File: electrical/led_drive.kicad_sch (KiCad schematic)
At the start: 0 parts

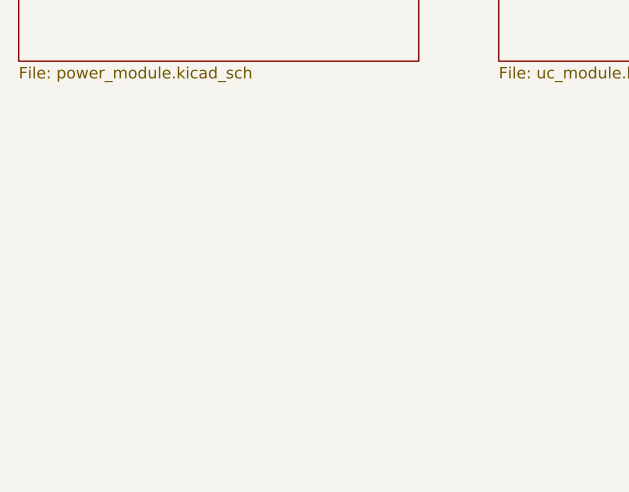
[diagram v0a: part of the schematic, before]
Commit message: Added more readme
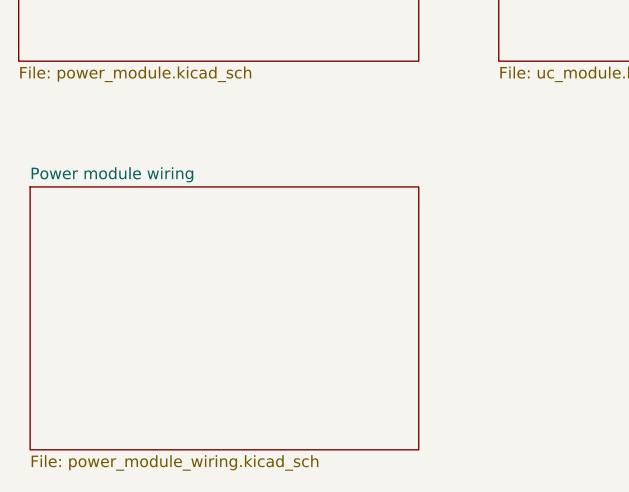
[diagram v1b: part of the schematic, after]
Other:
- added sheet Power module wiring (power_module_wiring.kicad_sch)
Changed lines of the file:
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@@
     (title "Bulb drive")
+  )
+  (sheet (at 27.94 81.28) (size 43.18 29.21) (fields_autoplaced)
+    (stroke (width 0.1524) (type solid))
+    (fill (color 0 0 0 0.0000))
+    (property "Sheetname" "Power module wiring" (at 27.94 80.5684 0)
+      (effects (font (size 1.27 1.27)) (justify left bottom))
+    )
+    (property "Sheetfile" "power_module_wiring.kicad_sch" (at 27.94 111.0746 0)
+      (effects (font (size 1.27 1.27)) (justify left top))
+    )
+    (instances
+      (project "led_drive"
+        (path "/01e69042-7c7e-48e9-b7c3-459316fd17f1" (page "6"))
+      )
+    )
   )
   (sheet (at 80.01 35.56) (size 45.72 31.75) (fields_autoplaced)

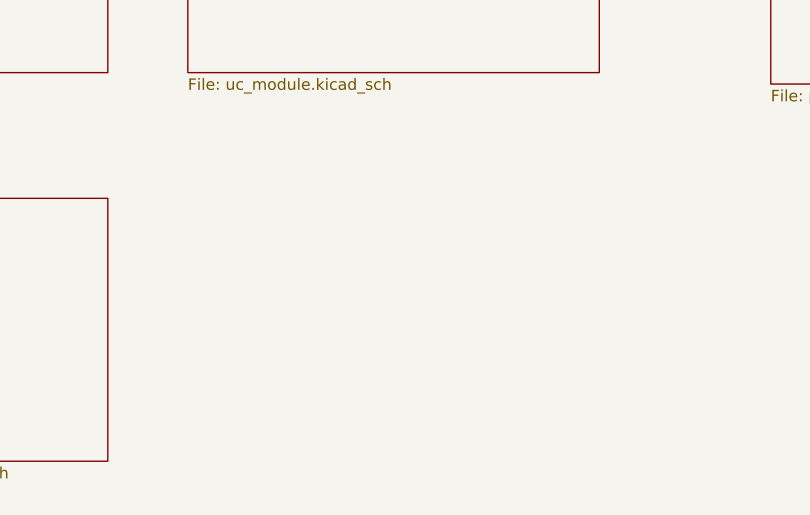
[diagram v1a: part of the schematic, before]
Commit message: Electrical diagram refactor
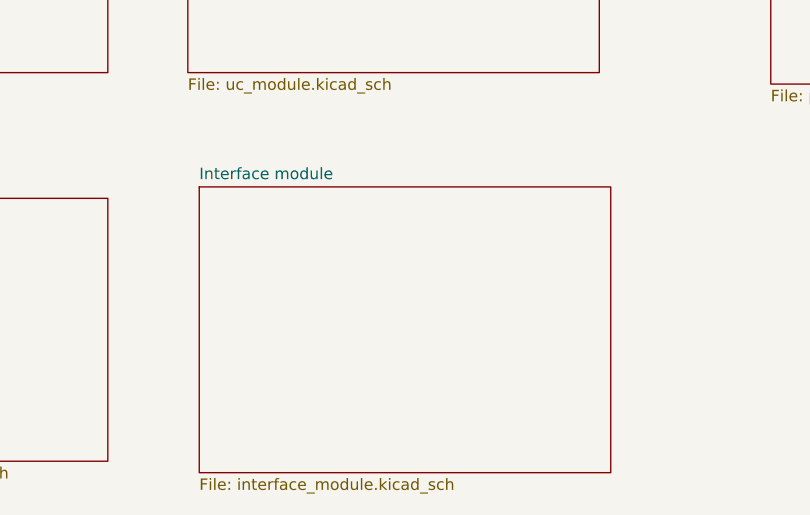
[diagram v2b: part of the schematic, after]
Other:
- added sheet Interface module (interface_module.kicad_sch)
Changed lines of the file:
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@@
+    )
+  )
+  (sheet (at 81.28 80.01) (size 45.72 31.75) (fields_autoplaced)
+    (stroke (width 0.1524) (type solid))
+    (fill (color 0 0 0 0.0000))
+    (property "Sheetname" "Interface module" (at 81.28 79.2984 0)
+      (effects (font (size 1.27 1.27)) (justify left bottom))
+    )
+    (property "Sheetfile" "interface_module.kicad_sch" (at 81.28 112.3446 0)
+      (effects (font (size 1.27 1.27)) (justify left top))
+    )
+    (instances
+      (project "led_drive"
+        (path "/01e69042-7c7e-48e9-b7c3-459316fd17f1" (page "2"))
+      )
     )
   )

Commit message: electrical module draft
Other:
- removed sheet Power module P
- added sheet Power delivery module (power_delivery_module.kicad_sch)
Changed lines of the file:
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@@
   (title_block
     (title "Bulb drive")
+    (date "2023-04-19")
   )
   (sheet (at 27.94 81.28) (size 43.18 29.21) (fields_autoplaced)
@@
     )
   )
+  (sheet (at 27.94 35.56) (size 45.72 31.75) (fields_autoplaced)
+    (stroke (width 0.1524) (type solid))
+    (fill (color 0 0 0 0.0000))
+    (property "Sheetname" "Power delivery module" (at 27.94 34.8484 0)
+      (effects (font (size 1.27 1.27)) (justify left bottom))
+    )
+    (property "Sheetfile" "power_delivery_module.kicad_sch" (at 27.94 67.8946 0)
+      (effects (font (size 1.27 1.27)) (justify left top))
+    )
+    (instances
+      (project "led_drive"
+        (path "/01e69042-7c7e-48e9-b7c3-459316fd17f1" (page "5"))
+      )
+    )
+  )
   (sheet (at 144.78 39.37) (size 36.83 29.21) (fields_autoplaced)
     (stroke (width 0.1524) (type solid))
@@
       )
     )
-  )
-  (sheet (at 26.67 34.29) (size 44.45 33.02) (fields_autoplaced)
-    (stroke (width 0.1524) (type solid))
-    (fill (color 0 0 0 0.0000))
-    (property "Sheetname" "Power module P" (at 26.67 33.5784 0)
-      (effects (font (size 1.27 1.27)) (justify left bottom))
-    )
-    (property "Sheetfile" "power_module.kicad_sch" (at 26.67 67.8946 0)
-      (effects (font (size 1.27 1.27)) (justify left top))
-    )
-    (instances
-      (project "led_drive"
-        (path "/01e69042-7c7e-48e9-b7c3-459316fd17f1" (page "5"))
-      )
-    )

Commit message: Względenie działa
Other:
- removed sheet Interface module
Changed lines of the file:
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@@
 	(title_block
 		(title "Bulb drive")
-		(date "2023-04-19")
+		(date "2024-04-14")
 	)
 	(sheet
@@
 	)
 	(sheet
-		(at 144.78 39.37)
+		(at 135.89 36.83)
 		(size 36.83 29.21)
 		(fields_autoplaced yes)
@@
 		)
 		(property "Sheetname" "Power module N"
-			(at 144.78 38.6584 0)
+			(at 135.89 36.1184 0)
 			(effects
 				(font
@@
 		)
 		(property "Sheetfile" "power_module_n.kicad_sch"
-			(at 144.78 69.1646 0)
+			(at 135.89 66.6246 0)
 			(effects
 				(font
@@
 				)
 			)
-		)
-	)
-	(sheet
-		(at 81.28 80.01)
-		(size 45.72 31.75)
-		(fields_autoplaced yes)
-		(stroke
-			(width 0.1524)
-			(type solid)
-		)
-		(fill
-			(color 0 0 0 0.0000)
-		)
-		(property "Sheetname" "Interface module"
-			(at 81.28 79.2984 0)
-			(effects
-				(font
-					(size 1.27 1.27)
-				)
-				(justify left bottom)
-			)
-		)
-		(property "Sheetfile" "interface_module.kicad_sch"
-			(at 81.28 112.3446 0)
-			(effects
-				(font
-					(size 1.27 1.27)
-				)
-				(justify left top)
-			)
-		)
-		(instances
-			(project "led_drive"
-				(path "/01e69042-7c7e-48e9-b7c3-459316fd17f1"
-					(page "2")
-				)
-			)
